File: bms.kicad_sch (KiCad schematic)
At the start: 19 parts, among them Q1 SSM6K513NU-LF, Q2 SSM6K513NU-LF, Q3 2N7002W, U1 BQ28Z620DRZR

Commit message: Batter scematic done.
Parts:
- added C6: 100nF, Capacitor_SMD:C_0603_1608Metric_Pad1.08x0.95mm_HandSolder, symbol Device:C
- added C7: 2.2uF, Capacitor_SMD:C_0603_1608Metric_Pad1.08x0.95mm_HandSolder, symbol Device:C
- added C8: 1uF, Capacitor_SMD:C_0603_1608Metric_Pad1.08x0.95mm_HandSolder, symbol Device:C
- added F1: Fuse, Resistor_SMD:R_0603_1608Metric_Pad0.98x0.95mm_HandSolder, symbol Device:Fuse
- added JP1, JP2: Jumper_2_Bridged, Connector_PinHeader_2.54mm:PinHeader_1x02_P2.54mm_Horizontal, symbol Jumper:Jumper_2_Bridged
- added R10, R11, R12: 100R, Resistor_SMD:R_0603_1608Metric_Pad0.98x0.95mm_HandSolder, symbol Device:R
- added R13: 5R, Resistor_SMD:R_0603_1608Metric_Pad0.98x0.95mm_HandSolder, symbol Device:R
- added TP1, TP2: TestPoint, TestPoint:TestPoint_Pad_D1.5mm, symbol Connector:TestPoint
- C1, C2: value C -> 100nF
- R5: value 5K1 -> 5R1
- R6: Size (none) -> 1608; Tolerance (none) -> 1%
- R8, R9: value 5K1 -> 100R
- TH1: value Thermistor_NTC -> NTCG103JH103JT1; Size (none) -> 0402
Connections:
- net Vcell- is gone; now on net CGND: R6.2, R8.1
- net Vcell+: now also F1.1; no longer C1.1, Q1.4, Q1.8, R1.2
- net Vpack+: now also C2.2, Q2.4, Q2.8, Q3.2, R2.2, R5.2
- net comm.SCL: now also JP1.2 (B); no longer U1.5 (SCL)
- net comm.SDA: now also JP2.2 (B); no longer U1.6 (SDA)
- net at Q1.1, Q1.2, Q1.5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: now also TP2.1
- net CGND: now reaches C3.2, C4.1
- net CGND: now also U1.1 (VSS), U1.13 (PWPD), C6.1, C7.1
- net at U1.10 (PBI): now also C7.2
- net at U1.11 (VC2): now also C8.1, R13.2
- net at U1.12 (VC1): now also C6.2, C8.2, R10.1
- net Vpack- renamed GNDPWR
- net GNDPWR: no longer U1.1 (VSS), U1.13 (PWPD)
- new net: C1.1, F1.2, Q1.4, Q1.8, R1.2, R10.2, R13.1, TP1.1
- new net: JP1.1 (A), R11.1
- new net: R11.2, U1.5 (SCL)
- new net: JP2.1 (A), R12.1
- new net: R12.2, U1.6 (SDA)
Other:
- note added: "Connector point for EV2400 and BQStudio."
- moved on the sheet: C3, C4, C5, Q3, R1, R2, R3, R4, R5, R6, R7, R8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

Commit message: Draw power schematic.
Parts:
- removed JP1, JP2: Jumper_2_Bridged, Connector_PinHeader_2.54mm:PinHeader_1x02_P2.54mm_Horizontal, symbol Jumper:Jumper_2_Bridged
- added J1: Conn_01x03_Pin, Connector_PinHeader_2.54mm:PinHeader_1x03_P2.54mm_Horizontal, symbol Connector:Conn_01x03_Pin
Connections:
- net GNDPWR: now also J1.1 (Pin_1)
- net comm.SCL: now also R11.1, J1.2 (Pin_2)
- net comm.SDA: now also R12.1, J1.3 (Pin_3)

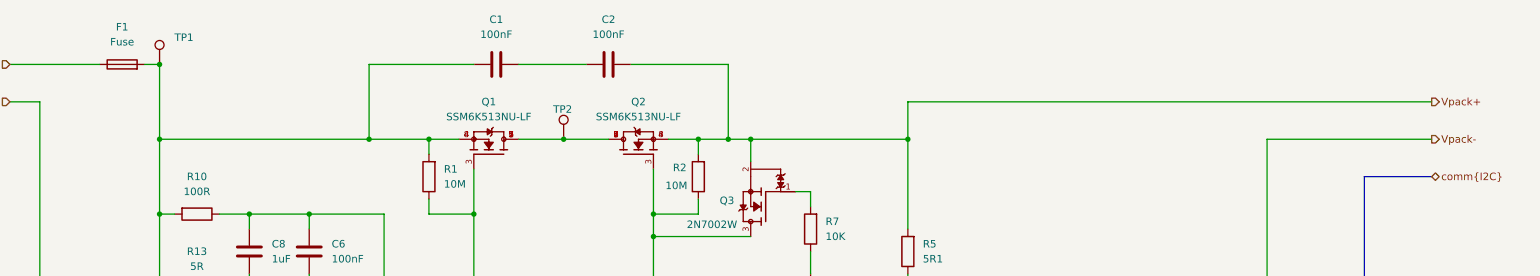
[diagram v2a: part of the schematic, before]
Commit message: Add charger, battery cell.
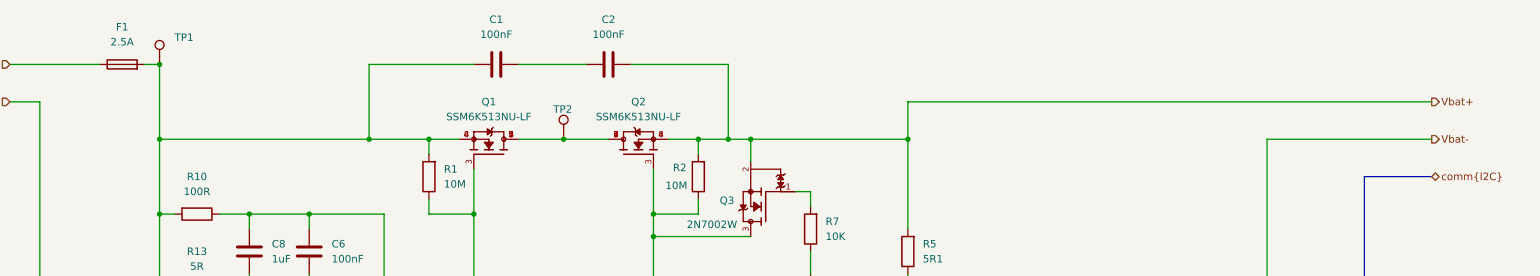
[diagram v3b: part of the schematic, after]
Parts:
- F1: value Fuse -> 2.5A
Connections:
- net Vpack+ renamed Vbat+
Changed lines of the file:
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@@
 		)
 	)
-	(hierarchical_label "Vpack-"
+	(hierarchical_label "Vbat-"
 		(shape output)
 		(at 266.7 38.1 0)
@@
 		)
 	)
-	(hierarchical_label "Vpack+"
+	(hierarchical_label "Vbat+"
 		(shape output)
 		(at 266.7 31.75 0)
@@
 			)
 		)
-		(property "Value" "Fuse"
+		(property "Value" "2.5A"
 			(at 44.45 21.59 90)
 			(show_name no)

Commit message: Fix issues
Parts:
- removed C8: 1uF, Capacitor_SMD:C_0603_1608Metric_Pad1.08x0.95mm_HandSolder, symbol Device:C
- removed J1: Conn_01x03_Pin, Connector_PinHeader_2.54mm:PinHeader_1x03_P2.54mm_Horizontal, symbol Connector:Conn_01x03_Pin
- removed R13: 5R, Resistor_SMD:R_0603_1608Metric_Pad0.98x0.95mm_HandSolder, symbol Device:R
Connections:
- net at U1.11 (VC2): now also C6.2, R10.1, U1.12 (VC1)
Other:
- note added: "Should be placed close to the cell!"
- note removed: "Connector point for EV2400 and BQStudio."
- moved on the sheet: C6

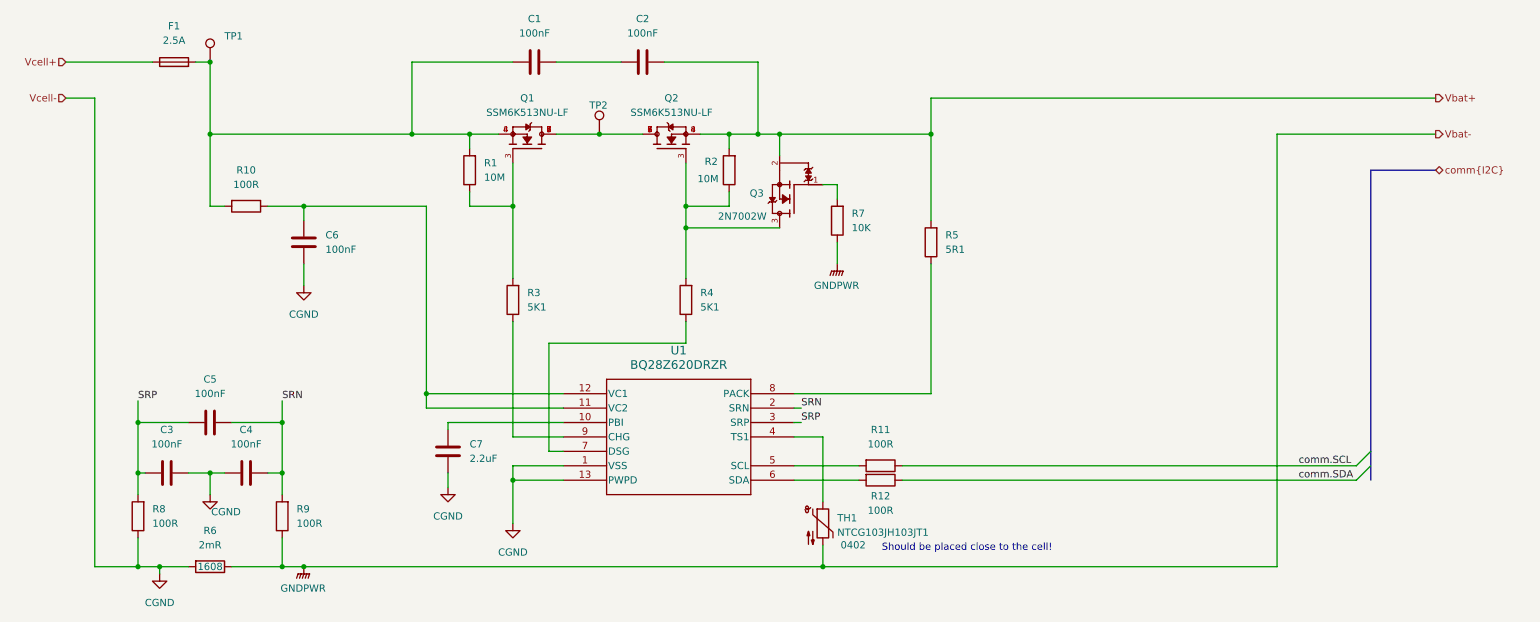
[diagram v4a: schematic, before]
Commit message: Fix issues from Issue#1
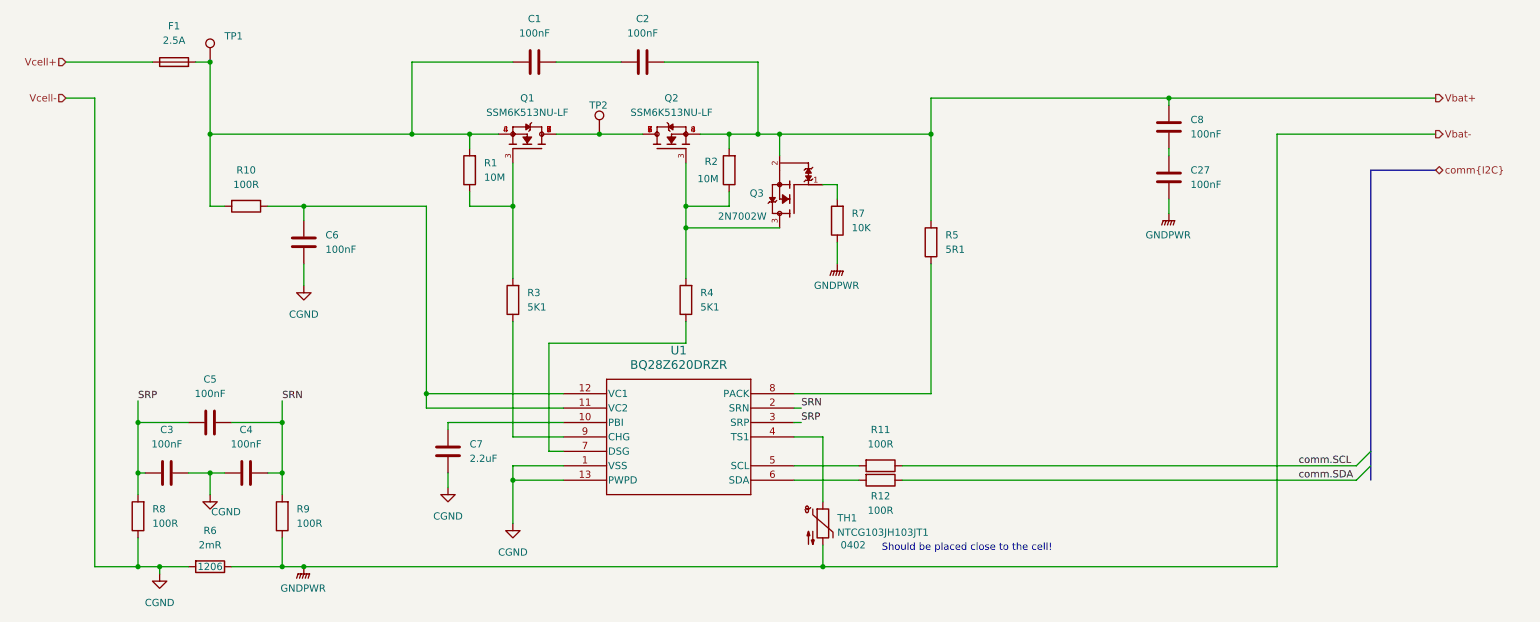
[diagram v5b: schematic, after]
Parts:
- added C27, C8: 100nF, Capacitor_SMD:C_0603_1608Metric_Pad1.08x0.95mm_HandSolder, symbol Device:C
- R6: Size 1608 -> 1206
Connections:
- net GNDPWR: now also C27.1
- net Vbat+: now also C8.2
- new net: C27.2, C8.1

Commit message: Fix wrong wiring, add pcb design.
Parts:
- removed TP1: TestPoint, TestPoint:TestPoint_Pad_D1.5mm, symbol Connector:TestPoint
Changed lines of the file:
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@@
-	)
-	(junction
-		(at 50.8 25.4)
-		(diameter 0)
-		(color 0 0 0 0)
 	)
 	(junction
@@
 	(wire
 		(pts
+			(xy 48.26 25.4) (xy 50.8 25.4)
+		)
+		(stroke
+			(width 0)
+			(type default)
+		)
+	)
+	(wire
+		(pts
 			(xy 104.14 96.52) (xy 104.14 99.06)
 		)
@@
 		(pts
 			(xy 104.14 91.44) (xy 113.03 91.44)
-		)
-		(stroke
-			(width 0)
-			(type default)
-		)
-	)
-	(wire
-		(pts
-			(xy 48.26 25.4) (xy 50.8 25.4)
 		)
 		(stroke
@@
 					(unit 1)
 				)
-			)
-		)
-	)
-	(symbol
-		(lib_id "Connector:TestPoint")
-		(at 50.8 25.4 0)
-		(unit 1)
-		(body_style 1)
-		(exclude_from_sim no)
-		(in_bom yes)
-		(on_board yes)
-		(in_pos_files yes)
-		(dnp no)
-		(fields_autoplaced yes)
-		(property "Reference" "TP1"
-			(at 53.34 20.8279 0)
-			(show_name no)
-			(do_not_autoplace no)
-			(effects
-				(font
-					(size 1.27 1.27)
-				)
-				(justify left)
-			)
-		)
-		(property "Value" "TestPoint"
-			(at 53.34 23.3679 0)
-			(hide yes)
-			(show_name no)
-			(do_not_autoplace no)
-			(effects
-				(font
-					(size 1.27 1.27)
-				)
-				(justify left)
-			)
-		)
-		(property "Footprint" "TestPoint:TestPoint_Pad_D1.5mm"
-			(at 55.88 25.4 0)
-			(hide yes)
-			(show_name no)
-			(do_not_autoplace no)
-			(effects
-				(font
-					(size 1.27 1.27)
-				)
-			)
-		)
-		(property "Datasheet" ""
-			(at 55.88 25.4 0)
-			(hide yes)
-			(show_name no)
-			(do_not_autoplace no)
-			(effects
-				(font
-					(size 1.27 1.27)
-				)
-			)
-		)
-		(property "Description" "test point"
-			(at 50.8 25.4 0)
-			(hide yes)
-			(show_name no)
-			(do_not_autoplace no)
-			(effects
-				(font
-					(size 1.27 1.27)
-				)
-			)
-		)
-		(pin "1"
-		)
-		(instances
-			(project "MoistureESP"
-				(path "/f2b9f638-139e-46ec-aa60-77c4af989196/b13ba67b-4069-4f36-b5d0-6a46a6b78ce9"
-					(reference "TP1")
-					(unit 1)
-				)

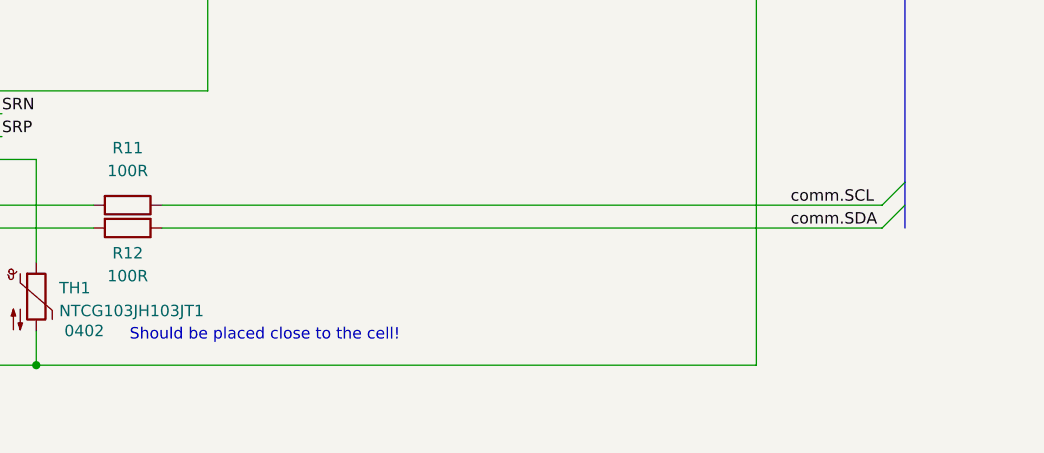
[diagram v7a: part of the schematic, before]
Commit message: Add footprint to debug connector.
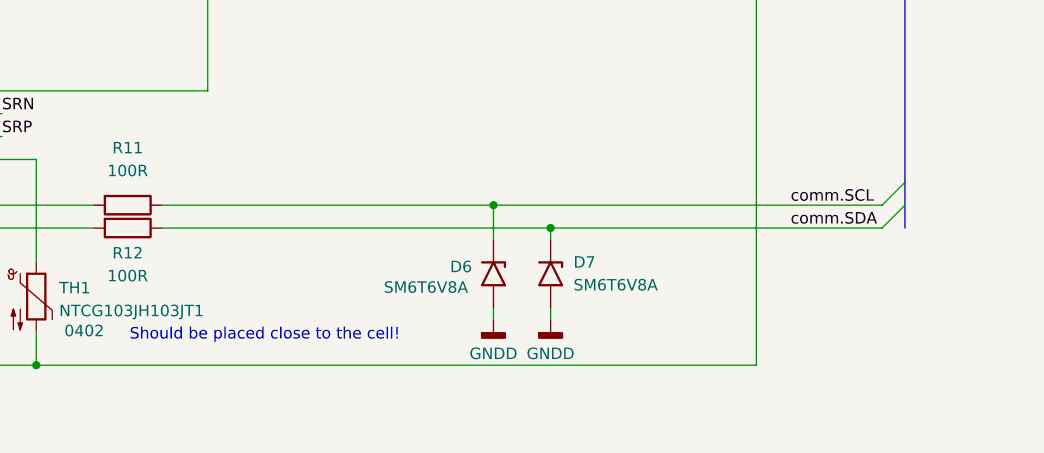
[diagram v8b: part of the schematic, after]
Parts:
- added D6, D7: SM6T6V8A, Diode_SMD:D_SMB, symbol Diode:SM6T6V8A
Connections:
- net comm.SCL: now also D6.1 (A1)
- net comm.SDA: now also D7.1 (A1)
- new net GNDD: D6.2 (A2), D7.2 (A2)
